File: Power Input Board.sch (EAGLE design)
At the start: 19 parts, among them Q1 SPB80P06P

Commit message: fixed some stuff
moved things around
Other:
- note added: "12V CONNECTORS"
- note added: "BOARD OUTLINE"
- note added: "OR-ING DIODES"
- note added: "POWER BRICK CONNECTORS"
- note added: "REVERSE VOLTAGE PROTECTION"
- note added: "TURN OFF/ON CIRCUIT"
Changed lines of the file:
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@@
 <sheet>
 <plain>
-<text x="30.48" y="106.68" size="2.54" layer="91">48 VOLT CONNECTOR</text>
+<text x="17.78" y="101.6" size="2.54" layer="91">48 VOLT CONNECTOR</text>
+<text x="81.28" y="111.76" size="2.54" layer="91">12V CONNECTORS</text>
+<text x="144.78" y="111.76" size="2.54" layer="91">POWER BRICK CONNECTORS</text>
+<text x="27.94" y="236.22" size="2.54" layer="91">TURN OFF/ON CIRCUIT</text>
+<text x="132.08" y="233.68" size="2.54" layer="91">REVERSE VOLTAGE PROTECTION</text>
+<text x="287.02" y="109.22" size="2.54" layer="91">BOARD OUTLINE</text>
+<text x="279.4" y="243.84" size="2.54" layer="91">OR-ING DIODES</text>
 </plain>
 <instances>
@@
 <attribute name="NAME" x="133.35" y="212.09" size="1.778" layer="95"/>
 </instance>
-<instance part="U$2" gate="G$1" x="215.9" y="241.3"/>
+<instance part="U$2" gate="G$1" x="299.72" y="101.6"/>
 <instance part="U$3" gate="G$1" x="284.48" y="213.36">
 <attribute name="NAME" x="284.48" y="218.44" size="1.778" layer="95"/>
@@
 <attribute name="VALUE" x="327.66" y="239.014" size="1.778" layer="96" align="bottom-center"/>
 </instance>
-<instance part="U$5" gate="G$1" x="297.18" y="147.32"/>
-<instance part="U$6" gate="G$1" x="297.18" y="119.38"/>
+<instance part="U$5" gate="G$1" x="160.02" y="81.28"/>
+<instance part="U$6" gate="G$1" x="160.02" y="53.34"/>
 <instance part="J1" gate="G$1" x="50.8" y="96.52">
 <attribute name="NAME" x="49.784" y="98.298" size="1.778" layer="95" font="vector"/>
@@
 <segment>
 <pinref part="U$5" gate="G$1" pin="ON/OFF"/>
-<wire x1="292.1" y1="149.86" x2="279.4" y2="149.86" width="0.1524" layer="91"/>
-<label x="276" y="150" size="1.778" layer="95"/>
+<wire x1="154.94" y1="83.82" x2="142.24" y2="83.82" width="0.1524" layer="91"/>
+<label x="138.84" y="83.96" size="1.778" layer="95"/>
 </segment>
 <segment>
 <pinref part="U$6" gate="G$1" pin="ON/OFF"/>
-<wire x1="292.1" y1="121.92" x2="279.4" y2="121.92" width="0.1524" layer="91"/>
-<label x="276" y="122" size="1.778" layer="95"/>
+<wire x1="154.94" y1="55.88" x2="142.24" y2="55.88" width="0.1524" layer="91"/>
+<label x="138.84" y="55.96" size="1.778" layer="95"/>
 </segment>
 </net>
@@
 <segment>
 <pinref part="U$5" gate="G$1" pin="+48V"/>
-<wire x1="325.12" y1="165.1" x2="337.82" y2="165.1" width="0.1524" layer="91"/>
-<label x="335" y="166" size="1.778" layer="95"/>
+<wire x1="187.96" y1="99.06" x2="200.66" y2="99.06" width="0.1524" layer="91"/>
+<label x="197.84" y="99.96" size="1.778" layer="95"/>
 </segment>
 <segment>
 <pinref part="U$6" gate="G$1" pin="+48V"/>
-<wire x1="325.12" y1="137.16" x2="337.82" y2="137.16" width="0.1524" layer="91"/>
-<label x="335" y="138" size="1.778" layer="95"/>
+<wire x1="187.96" y1="71.12" x2="200.66" y2="71.12" width="0.1524" layer="91"/>
+<label x="197.84" y="71.96" size="1.778" layer="95"/>
 </segment>
 </net>
@@
 <segment>
 <pinref part="U$5" gate="G$1" pin="+12V"/>
-<wire x1="292.1" y1="165.1" x2="279.4" y2="165.1" width="0.1524" layer="91"/>
-<label x="276.32" y="166.1" size="1.778" layer="95"/>
+<wire x1="154.94" y1="99.06" x2="142.24" y2="99.06" width="0.1524" layer="91"/>
+<label x="139.16" y="100.06" size="1.778" layer="95"/>
 </segment>
 </net>
@@
 <segment>
 <pinref part="U$6" gate="G$1" pin="+12V"/>
-<wire x1="292.1" y1="137.16" x2="279.4" y2="137.16" width="0.1524" layer="91"/>
-<label x="276" y="138" size="1.778" layer="95"/>
+<wire x1="154.94" y1="71.12" x2="142.24" y2="71.12" width="0.1524" layer="91"/>
+<label x="138.84" y="71.96" size="1.778" layer="95"/>
 </segment>
 </net>
@@
 <segment>
 <pinref part="U$5" gate="G$1" pin="GND"/>
-<wire x1="292.1" y1="157.48" x2="279.4" y2="157.48" width="0.1524" layer="91"/>
-<label x="278" y="158" size="1.778" layer="95"/>
+<wire x1="154.94" y1="91.44" x2="142.24" y2="91.44" width="0.1524" layer="91"/>
+<label x="140.84" y="91.96" size="1.778" layer="95"/>
 </segment>
 <segment>
 <pinref part="U$6" gate="G$1" pin="GND"/>
-<wire x1="292.1" y1="129.54" x2="279.4" y2="129.54" width="0.1524" layer="91"/>
-<label x="276" y="130" size="1.778" layer="95"/>
+<wire x1="154.94" y1="63.5" x2="142.24" y2="63.5" width="0.1524" layer="91"/>
+<label x="138.84" y="63.96" size="1.778" layer="95"/>
 </segment>
 <segment>
@@
 <segment>
 <pinref part="U$5" gate="G$1" pin="D_GND"/>
-<wire x1="325.12" y1="149.86" x2="337.82" y2="149.86" width="0.1524" layer="91"/>
+<wire x1="187.96" y1="83.82" x2="200.66" y2="83.82" width="0.1524" layer="91"/>
 </segment>
 </net>
@@
 <segment>
 <pinref part="U$6" gate="G$1" pin="D_GND"/>
-<wire x1="325.12" y1="121.92" x2="337.82" y2="121.92" width="0.1524" layer="91"/>
+<wire x1="187.96" y1="55.88" x2="200.66" y2="55.88" width="0.1524" layer="91"/>
 </segment>
 </net>
@@
 <segment>
 <pinref part="U$5" gate="G$1" pin="48V_GND"/>
-<wire x1="325.12" y1="157.48" x2="337.82" y2="157.48" width="0.1524" layer="91"/>
-<label x="335.28" y="157.48" size="1.778" layer="95"/>
+<wire x1="187.96" y1="91.44" x2="200.66" y2="91.44" width="0.1524" layer="91"/>
+<label x="198.12" y="91.44" size="1.778" layer="95"/>
 </segment>
 <segment>
 <pinref part="U$6" gate="G$1" pin="48V_GND"/>
-<wire x1="325.12" y1="129.54" x2="337.82" y2="129.54" width="0.1524" layer="91"/>
-<label x="335.28" y="129.54" size="1.778" layer="95"/>
-</segment>
-</net>
+<wire x1="187.96" y1="63.5" x2="200.66" y2="63.5" width="0.1524" layer="91"/>
+<label x="198.12" y="63.5" size="1.778" layer="95"/>
+</segment>
+</net>

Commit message: rerouted
rerouted everything
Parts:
- removed U$8, U$9: PDB_PCB_CONNEC, PDB_PCB_connectors:PDB_PCB_CONNEC
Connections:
- net +12V: no longer U$8.+12V, U$9.+12V
- net GND: no longer U$8.GND, U$9.GND
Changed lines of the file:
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@@
 <part name="J2" library="SparkFun-Connectors" deviceset="BANANA_CONN" device=""/>
 <part name="U$7" library="PDB_PCB_connectors" deviceset="PDB_PCB_CONNEC" device=""/>
-<part name="U$8" library="PDB_PCB_connectors" deviceset="PDB_PCB_CONNEC" device=""/>
-<part name="U$9" library="PDB_PCB_connectors" deviceset="PDB_PCB_CONNEC" device=""/>
 </parts>
 <sheets>
@@
 <attribute name="VALUE" x="49.784" y="88.392" size="1.778" layer="96" font="vector"/>
 </instance>
-<instance part="U$7" gate="G$1" x="99.06" y="86.36"/>
-<instance part="U$8" gate="G$1" x="99.06" y="63.5"/>
-<instance part="U$9" gate="G$1" x="99.06" y="40.64"/>
+<instance part="U$7" gate="G$1" x="93.98" y="81.28"/>
 </instances>
 <busses>
@@
 <segment>
 <pinref part="U$7" gate="G$1" pin="+12V"/>
-<wire x1="93.98" y1="101.6" x2="78.74" y2="101.6" width="0.1524" layer="91"/>
-<label x="78.74" y="101.6" size="1.778" layer="95"/>
-</segment>
-<segment>
-<pinref part="U$8" gate="G$1" pin="+12V"/>
-<wire x1="93.98" y1="78.74" x2="78.74" y2="78.74" width="0.1524" layer="91"/>
-<label x="78.74" y="78.74" size="1.778" layer="95"/>
-</segment>
-<segment>
-<pinref part="U$9" gate="G$1" pin="+12V"/>
-<wire x1="93.98" y1="55.88" x2="78.74" y2="55.88" width="0.1524" layer="91"/>
-<label x="78.74" y="55.88" size="1.778" layer="95"/>
+<wire x1="88.9" y1="96.52" x2="73.66" y2="96.52" width="0.1524" layer="91"/>
+<label x="73.66" y="96.52" size="1.778" layer="95"/>
 </segment>
 </net>
@@
 <segment>
 <pinref part="U$7" gate="G$1" pin="GND"/>
-<wire x1="93.98" y1="91.44" x2="78.74" y2="91.44" width="0.1524" layer="91"/>
-<label x="78.74" y="91.44" size="1.778" layer="95"/>
-</segment>
-<segment>
-<pinref part="U$8" gate="G$1" pin="GND"/>
-<wire x1="93.98" y1="68.58" x2="78.74" y2="68.58" width="0.1524" layer="91"/>
-<label x="78.74" y="68.58" size="1.778" layer="95"/>
-</segment>
-<segment>
-<pinref part="U$9" gate="G$1" pin="GND"/>
-<wire x1="93.98" y1="45.72" x2="78.74" y2="45.72" width="0.1524" layer="91"/>
-<label x="78.74" y="45.72" size="1.778" layer="95"/>
-</segment>
-</net>
+<wire x1="88.9" y1="86.36" x2="73.66" y2="86.36" width="0.1524" layer="91"/>
+<label x="73.66" y="86.36" size="1.778" layer="95"/>
+</segment>
+</net>

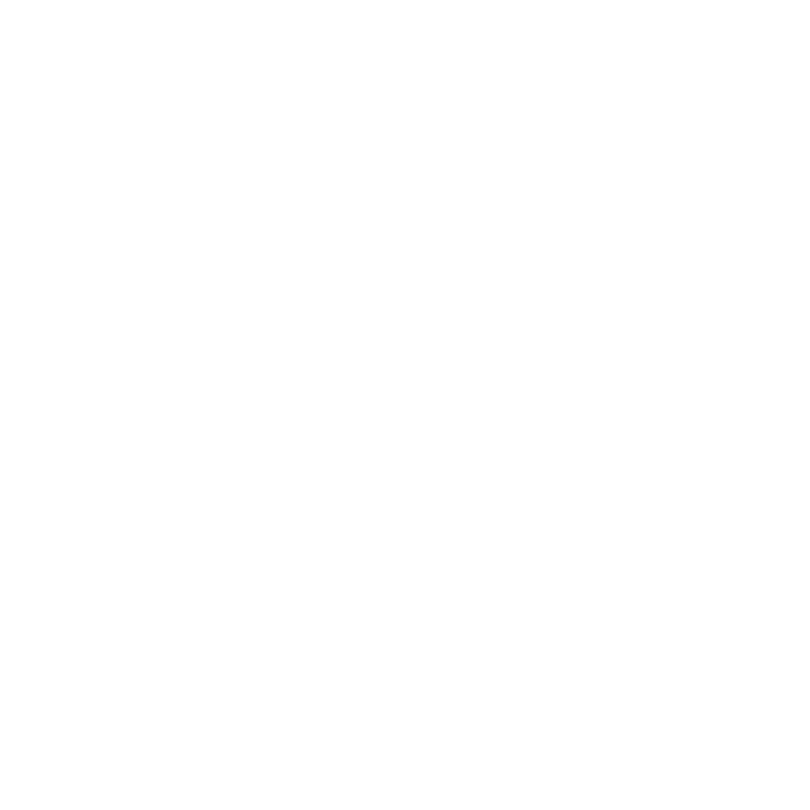
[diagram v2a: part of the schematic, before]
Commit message: added LED
added LED between 12V and GND
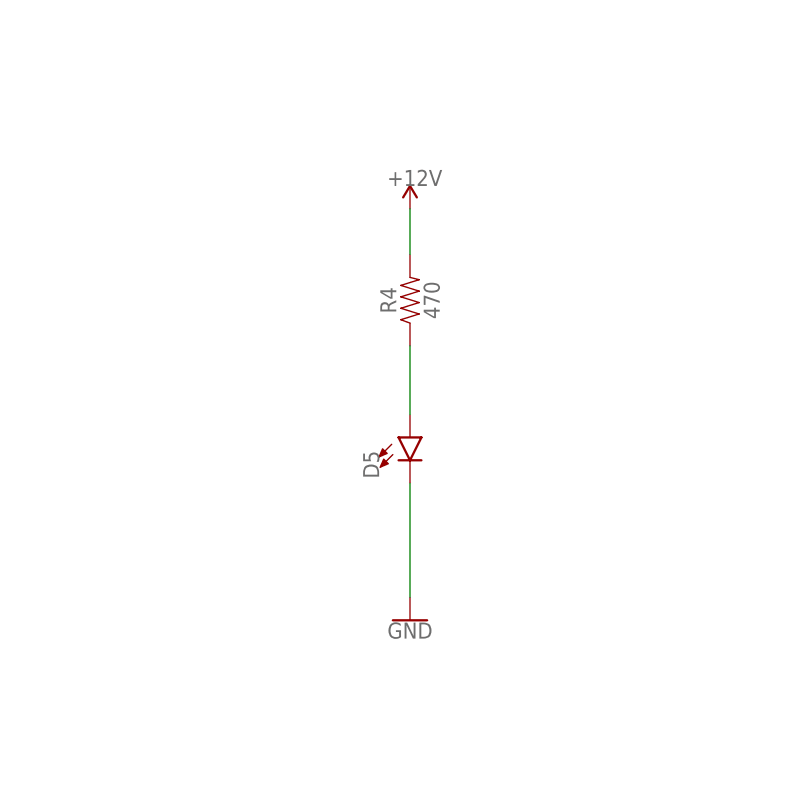
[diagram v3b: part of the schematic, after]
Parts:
- added D5: (no value), SparkFun-LED:LED0603
- added R4: 470, SparkFun-Resistors:RESISTOR0603
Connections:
- new net N$4: D5.A, R4.1
- net +12V: now also R4.2
- net GND: now also D5.C
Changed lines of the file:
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@@
 <part name="J2" library="SparkFun-Connectors" deviceset="BANANA_CONN" device=""/>
 <part name="U$7" library="PDB_PCB_connectors" deviceset="PDB_PCB_CONNEC" device=""/>
+<part name="D5" library="SparkFun-LED" library_urn="urn:adsk.eagle:library:529" deviceset="LED" device="0603" package3d_urn="urn:adsk.eagle:package:39354/1"/>
+<part name="R4" library="SparkFun-Resistors" library_urn="urn:adsk.eagle:library:532" deviceset="RESISTOR" device="0603" package3d_urn="urn:adsk.eagle:package:39650/1" value="470"/>
+<part name="GND2" library="SparkFun-PowerSymbols" library_urn="urn:adsk.eagle:library:530" deviceset="GND" device=""/>
+<part name="SUPPLY3" library="SparkFun-PowerSymbols" library_urn="urn:adsk.eagle:library:530" deviceset="VCCIO" device="" value=""/>
 </parts>
 <sheets>
@@
 </instance>
 <instance part="U$7" gate="G$1" x="93.98" y="81.28"/>
+<instance part="D5" gate="G$1" x="231.14" y="190.5">
+<attribute name="NAME" x="227.711" y="185.928" size="1.778" layer="95" font="vector" rot="R90"/>
+<attribute name="VALUE" x="233.045" y="185.928" size="1.778" layer="96" font="vector" rot="R90" align="top-left"/>
+</instance>
+<instance part="R4" gate="G$1" x="231.14" y="205.74" rot="R90">
+<attribute name="NAME" x="229.616" y="205.74" size="1.778" layer="95" font="vector" rot="R90" align="bottom-center"/>
+<attribute name="VALUE" x="232.664" y="205.74" size="1.778" layer="96" font="vector" rot="R90" align="top-center"/>
+</instance>
+<instance part="GND2" gate="1" x="231.14" y="170.18">
+<attribute name="VALUE" x="231.14" y="169.926" size="1.778" layer="96" align="top-center"/>
+</instance>
+<instance part="SUPPLY3" gate="G$1" x="231.14" y="215.9">
+<attribute name="VALUE" x="231.14" y="218.694" size="1.778" layer="96" align="bottom-center"/>
+</instance>
 </instances>
 <busses>
@@
 <label x="73.66" y="96.52" size="1.778" layer="95"/>
 </segment>
+<segment>
+<pinref part="R4" gate="G$1" pin="2"/>
+<pinref part="SUPPLY3" gate="G$1" pin="VCCIO"/>
+<wire x1="231.14" y1="210.82" x2="231.14" y2="215.9" width="0.1524" layer="91"/>
+<label x="228.6" y="218.44" size="1.778" layer="95"/>
+</segment>
 </net>
 <net name="GND" class="0">
@@
 <wire x1="88.9" y1="86.36" x2="73.66" y2="86.36" width="0.1524" layer="91"/>
 <label x="73.66" y="86.36" size="1.778" layer="95"/>
+</segment>
+<segment>
+<pinref part="GND2" gate="1" pin="GND"/>
+<pinref part="D5" gate="G$1" pin="C"/>
+<wire x1="231.14" y1="172.72" x2="231.14" y2="185.42" width="0.1524" layer="91"/>
 </segment>
 </net>
@@
 </segment>
 </net>
+<net name="N$4" class="0">
+<segment>
+<pinref part="D5" gate="G$1" pin="A"/>
+<pinref part="R4" gate="G$1" pin="1"/>
+<wire x1="231.14" y1="193.04" x2="231.14" y2="200.66" width="0.1524" layer="91"/>
+</segment>
+</net>

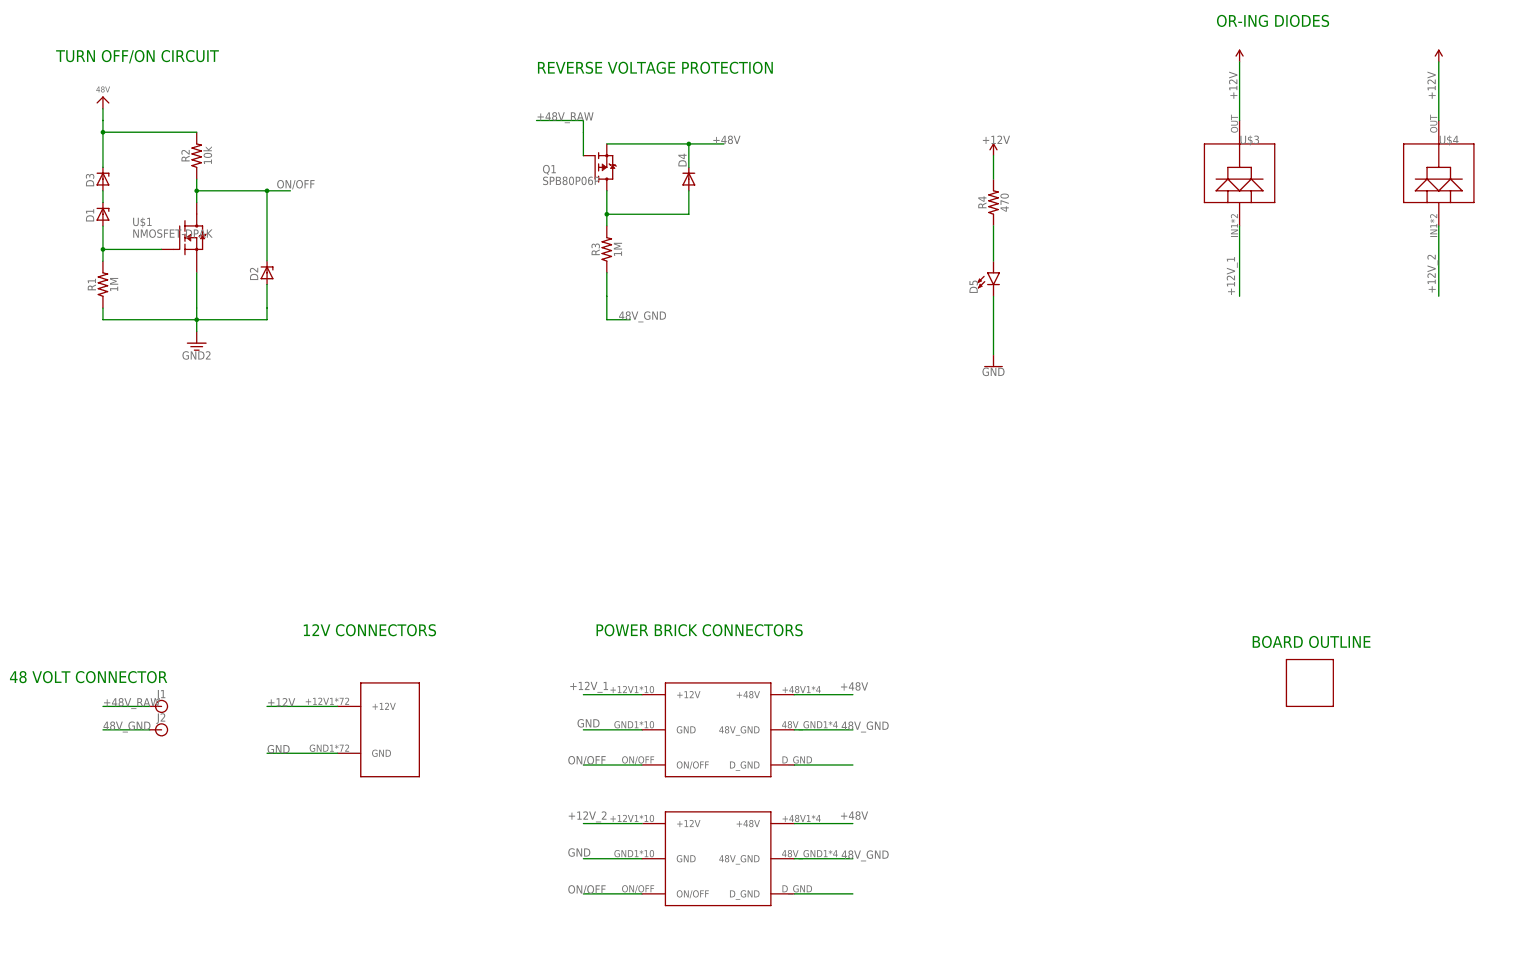
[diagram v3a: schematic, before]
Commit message: repositioning components
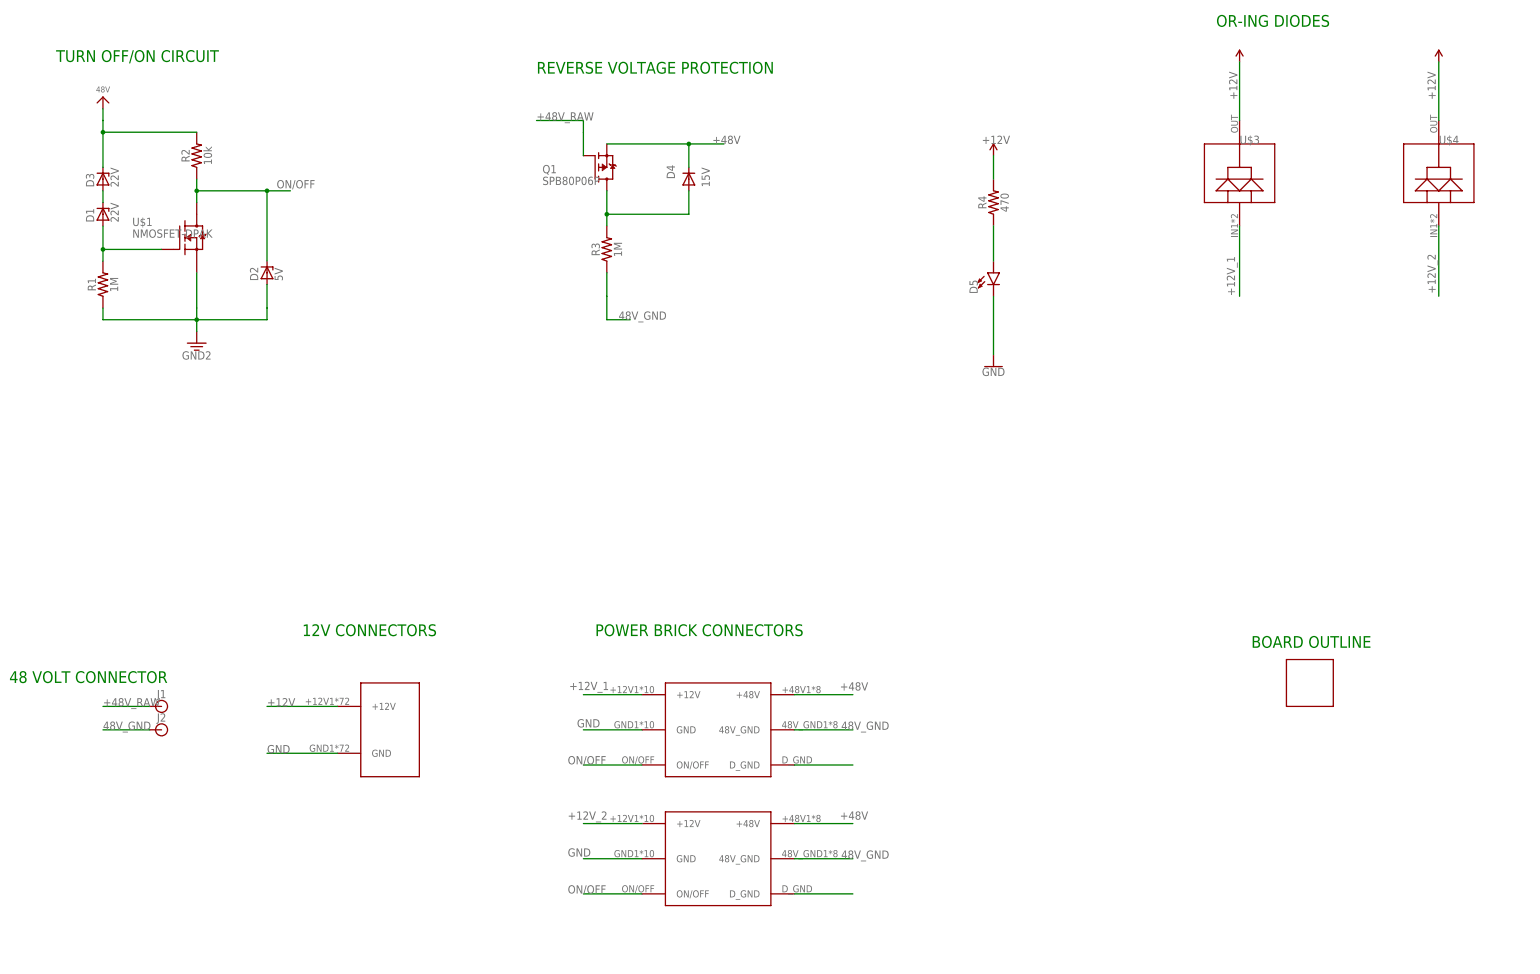
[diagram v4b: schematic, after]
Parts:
- D1, D3: value (none) -> 22V
- D2: value (none) -> 5V
- D4: value (none) -> 15V
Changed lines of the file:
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@@
 <parts>
 <part name="U$1" library="MotherboardParts" deviceset="NMOSFET-DPAK" device=""/>
-<part name="D1" library="diode" library_urn="urn:adsk.eagle:library:210" deviceset="ZENER-DIODE" device="SOT23" package3d_urn="urn:adsk.eagle:package:43389/2"/>
-<part name="D2" library="diode" library_urn="urn:adsk.eagle:library:210" deviceset="ZENER-DIODE" device="SOT23" package3d_urn="urn:adsk.eagle:package:43389/2"/>
-<part name="D3" library="diode" library_urn="urn:adsk.eagle:library:210" deviceset="ZENER-DIODE" device="SOT23" package3d_urn="urn:adsk.eagle:package:43389/2"/>
+<part name="D1" library="diode" library_urn="urn:adsk.eagle:library:210" deviceset="ZENER-DIODE" device="SOT23" package3d_urn="urn:adsk.eagle:package:43389/2" value="22V"/>
+<part name="D2" library="diode" library_urn="urn:adsk.eagle:library:210" deviceset="ZENER-DIODE" device="SOT23" package3d_urn="urn:adsk.eagle:package:43389/2" value="5V"/>
+<part name="D3" library="diode" library_urn="urn:adsk.eagle:library:210" deviceset="ZENER-DIODE" device="SOT23" package3d_urn="urn:adsk.eagle:package:43389/2" value="22V"/>
 <part name="R1" library="SparkFun-Resistors" library_urn="urn:adsk.eagle:library:532" deviceset="RESISTOR" device="0603" package3d_urn="urn:adsk.eagle:package:39650/1" value="1M">
 <attribute name="SPICEPREFIX" value="R"/>
@@
 <part name="P+1" library="audio amplifier example" library_urn="urn:adsk.eagle:library:970892" deviceset="VCC" device="" value="48V"/>
 <part name="GND1" library="SparkFun-PowerSymbols" library_urn="urn:adsk.eagle:library:530" deviceset="GND2" device=""/>
-<part name="D4" library="diode" library_urn="urn:adsk.eagle:library:210" deviceset="DIODE-" device="SOD123" package3d_urn="urn:adsk.eagle:package:43420/1"/>
+<part name="D4" library="diode" library_urn="urn:adsk.eagle:library:210" deviceset="DIODE-" device="SOD123" package3d_urn="urn:adsk.eagle:package:43420/1" value="15V"/>
 <part name="R3" library="SparkFun-Resistors" library_urn="urn:adsk.eagle:library:532" deviceset="RESISTOR" device="0603" package3d_urn="urn:adsk.eagle:package:39650/1" value="1M">
 <attribute name="SPICEPREFIX" value="R"/>
@@
 </instance>
 <instance part="D4" gate="G$1" x="165.1" y="210.82" rot="R90">
-<attribute name="NAME" x="164.6174" y="213.36" size="1.778" layer="95" rot="R90"/>
-<attribute name="VALUE" x="167.4114" y="213.36" size="1.778" layer="96" rot="R90"/>
+<attribute name="NAME" x="162.0774" y="210.82" size="1.778" layer="95" rot="R90"/>
+<attribute name="VALUE" x="167.8686" y="213.36" size="1.778" layer="96" rot="R270"/>
 </instance>
 <instance part="R3" gate="G$1" x="147.32" y="195.58" rot="R90">
